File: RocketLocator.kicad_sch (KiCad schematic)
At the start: 102 parts, among them J1 USB_C, J12 Battery / Switch, J2 Deploy Ch1 / Ch2, J3 Battery-, J4 Deploy Ch3 / Ch4, J7 U.FL-R-SMT(01), J8 Conn_ST_STDC14, Q1 2N7002KN, Q3 BSS84, U1 TPS22950YBHR, U11 PAM8904EGPR, U12 74HCS00, U13 DMP2021UFDF, U14 ISM6HG256XTR, U15 TPS22950YBHR, U16 MS5611-01BA, U17 MX25L6436F, U18 BQ25185DLHR, U2 SAM-M10Q-00B, U3 DRV5032DUDMRR, U4 CH340N, U5 STM32WL5MOCH6TR, U6 TPS22950YBHR, U7 RT9080-33GJ5, U8 TPS22950YBHR, U9 TPS22950YBHR

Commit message: Bundle project symbol and footprint libraries (#10)
* Bundle project symbol and footprint libraries

Adds the Custom symbol and footprint libraries from the personal KiCad 9.0
library folder, plus RT9080-33GJ5, STM32WL5MOCH6TR and U.FL-R-SMT_01_
symbols extracted from the schematic's embedded cache. Registers them in
project lib tables via ${KIPRJMOD} and adds a CI step that loads every
library so a broken file fails the build.

Co-Authored-By: Claude Opus 5.5 (1M context) <noreply@anthropic.com>
Claude-Session: https://claude.ai/code/session_01C1wUevCmefHv8PBPpeosyX

* Recover U7 and U17 footprints into Custom.pretty and relink

The RT9080 and Package_SO_New libraries are gone, so the footprints
were extracted from RocketLocator.kicad_pcb, un-flipped from B.Cu to
library (F.Cu) form, and added to lib/Custom.pretty. The schematic,
PCB and RT9080-33GJ5 symbol now point at Custom:.

Co-Authored-By: Claude Opus 5.5 (1M context) <noreply@anthropic.com>
Claude-Session: https://claude.ai/code/session_01C1wUevCmefHv8PBPpeosyX

---------

Co-authored-by: Claude <noreply@anthropic.com>
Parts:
- U17: footprint Package_SO_New:SOP-8_5.28x5.23mm_P1.27mm -> Custom:SOP-8_5.28x5.23mm_P1.27mm
- U7: footprint RT9080:SOT94P280X100-5N -> Custom:SOT94P280X100-5N
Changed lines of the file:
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@@
 			)
 		)
-		(property "Footprint" "RT9080:SOT94P280X100-5N"
+		(property "Footprint" "Custom:SOT94P280X100-5N"
 			(at 237.49 35.56 0)
 			(hide yes)
@@
 			)
 		)
-		(property "Footprint" "Package_SO_New:SOP-8_5.28x5.23mm_P1.27mm"
+		(property "Footprint" "Custom:SOP-8_5.28x5.23mm_P1.27mm"
 			(at 379.73 231.14 0)
 			(hide yes)

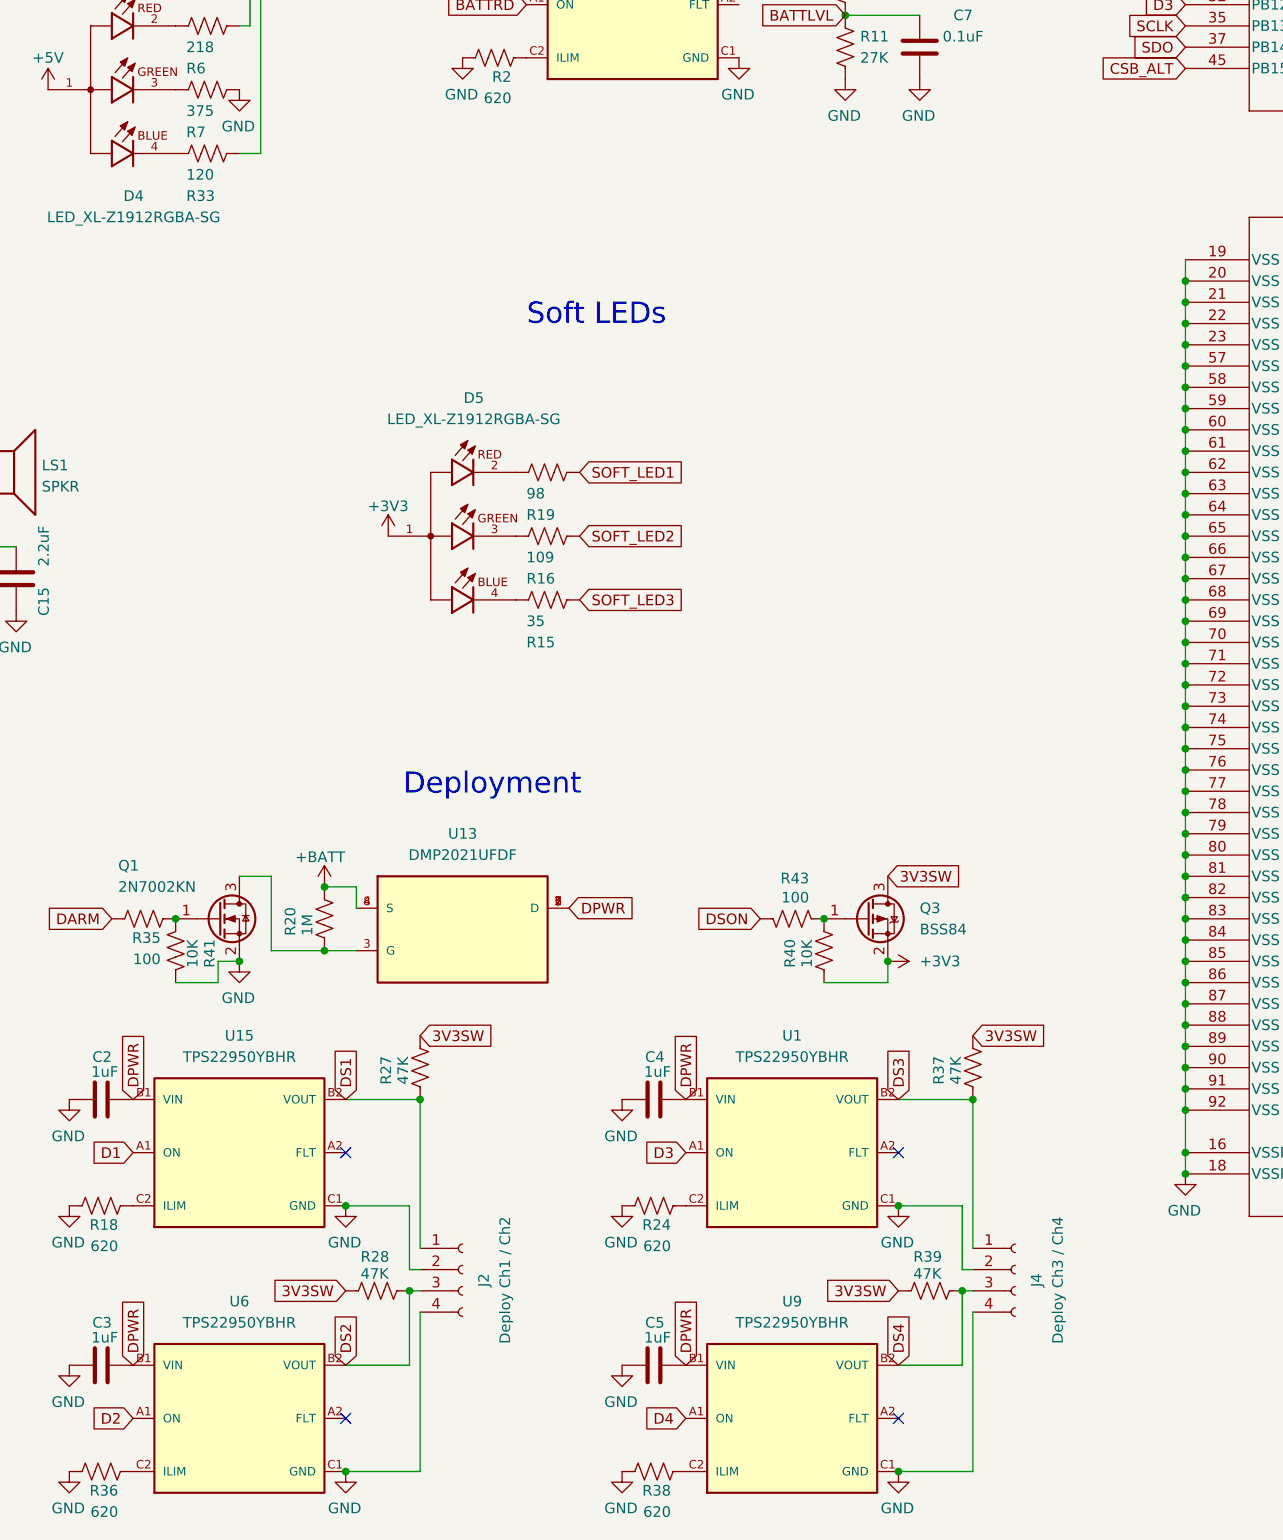
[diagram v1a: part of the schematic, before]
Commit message: Switch deploy returns low-side so continuity sense works (Topology A)
Each deploy channel's e-match return (J2/J4 pins 2 and 4) now goes through
an AO3400A low-side N-FET (Q4-Q7) instead of straight to GND. The gate is
driven from the same Dn GPIO as the TPS22950 ON pin through 100R, with a
100K pull-down. The DSn sense net and its existing 47K pull-up (R27, R28,
R37, R39) move to the FET drain, so the TPS22950 quick output discharge no
longer pins the sense node low. Each TPS22950 output (now DEPLOYn+) gets a
1K bleeder to GND (R53-R56).

The Soft LEDs block moved 25.4 mm left to make room for the new block.
The PCB still needs Update PCB from Schematic, placement and routing.

Fixes #1

Co-Authored-By: Claude Opus 5.5 (1M context) <noreply@anthropic.com>
Claude-Session: https://claude.ai/code/session_01MkgwVw8wg6ywYfkGV7BwAK
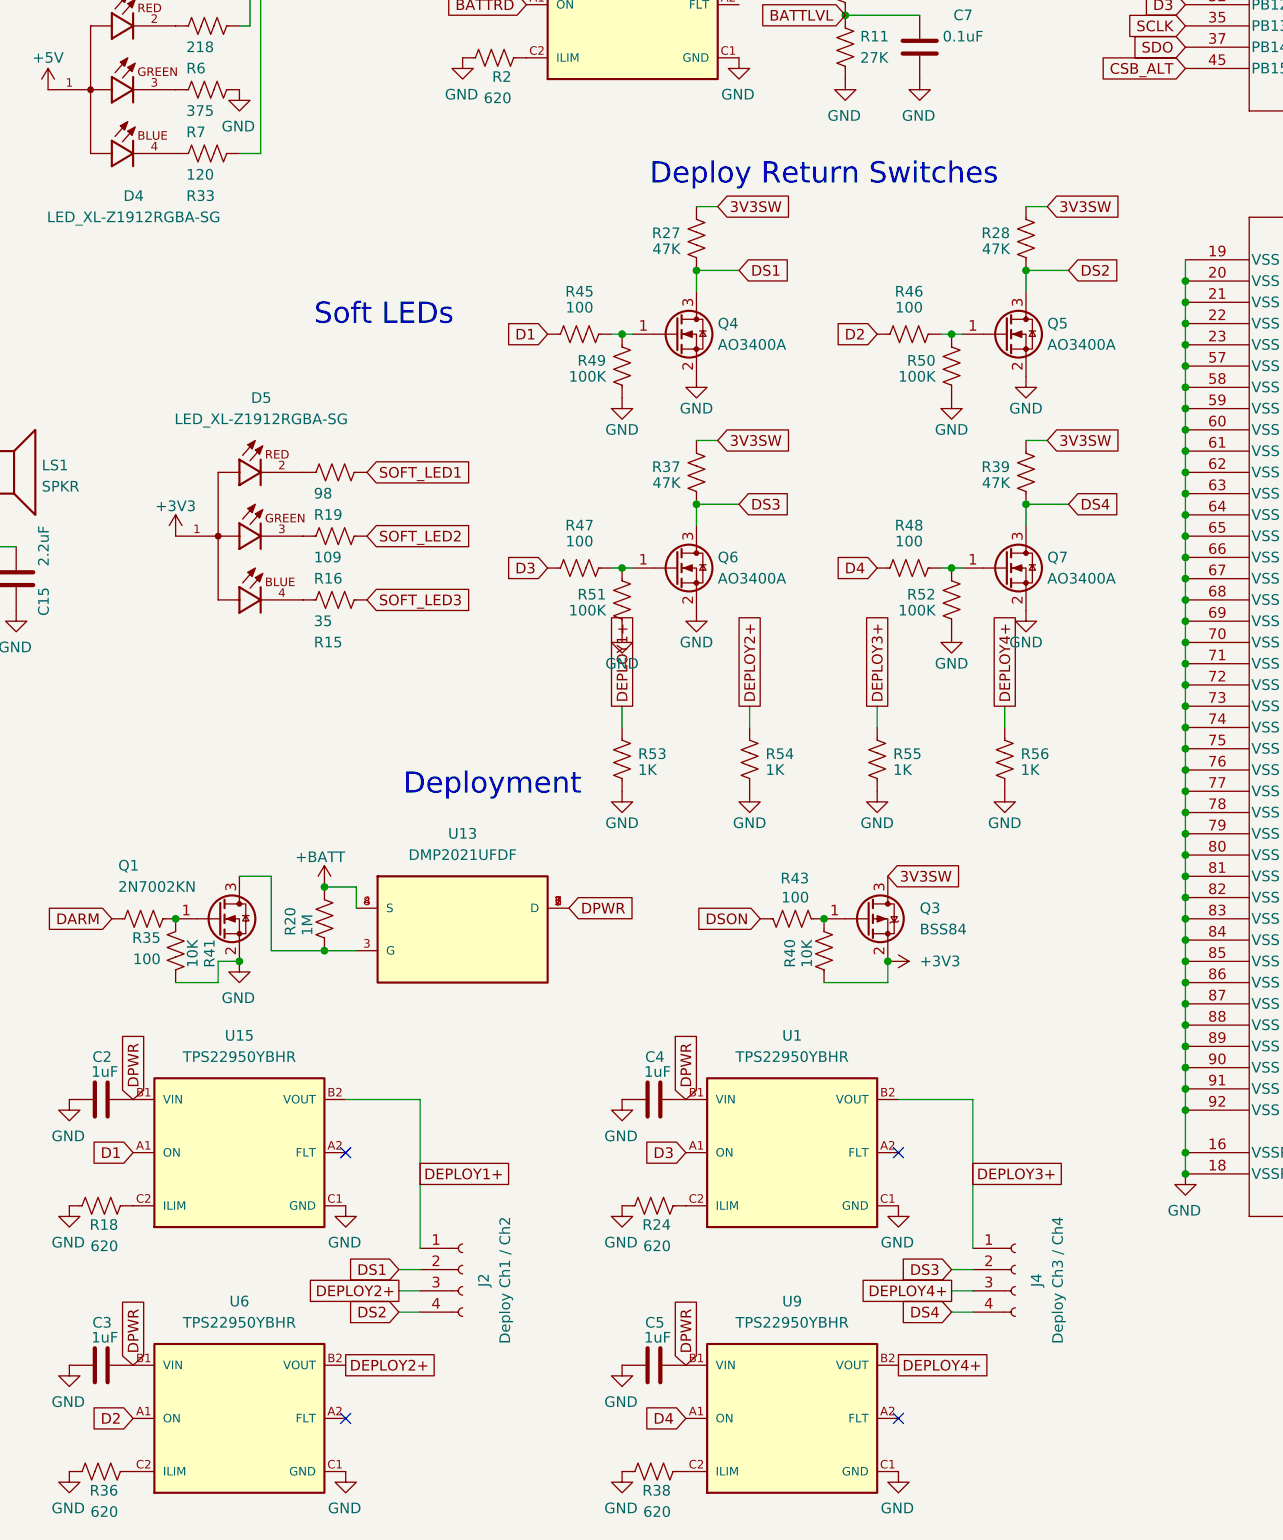
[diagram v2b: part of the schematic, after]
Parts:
- added Q4, Q5, Q6, Q7: AO3400A, Package_TO_SOT_SMD:SOT-23, symbol Transistor_FET:AO3400A
- added R45, R46, R47, R48: 100, Resistor_SMD:R_0402_1005Metric, symbol Device:R_US
- added R49, R50, R51, R52: 100K, Resistor_SMD:R_0402_1005Metric, symbol Device:R_US
- added R53, R54, R55, R56: 1K, Resistor_SMD:R_0402_1005Metric, symbol Device:R_US
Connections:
- net D1: now also R45.2
- net D2: now also R46.2
- net D3: now also R47.2
- net D4: now also R48.2
- net DS1: now also J2.2 (Pin_2), Q4.3 (D); no longer J2.1 (Pin_1), U15.B2 (VOUT)
- net DS2: now also J2.4 (Pin_4), Q5.3 (D); no longer J2.3 (Pin_3), U6.B2 (VOUT)
- net DS3: now also J4.2 (Pin_2), Q6.3 (D); no longer J4.1 (Pin_1), U1.B2 (VOUT)
- net DS4: now also J4.4 (Pin_4), Q7.3 (D); no longer J4.3 (Pin_3), U9.B2 (VOUT)
- net GND: now also Q4.2 (S), Q5.2 (S), Q6.2 (S), Q7.2 (S), R49.2, R50.2, R51.2, R52.2, R53.2, R54.2, R55.2, R56.2; no longer J2.2 (Pin_2), J2.4 (Pin_4), J4.2 (Pin_2), J4.4 (Pin_4)
- new net: Q5.1 (G), R46.1, R50.1
- new net: Q4.1 (G), R45.1, R49.1
- new net: Q7.1 (G), R48.1, R52.1
- new net: Q6.1 (G), R47.1, R51.1
- new net DEPLOY1+: J2.1 (Pin_1), R53.1, U15.B2 (VOUT)
- new net DEPLOY2+: J2.3 (Pin_3), R54.1, U6.B2 (VOUT)
- new net DEPLOY3+: J4.1 (Pin_1), R55.1, U1.B2 (VOUT)
- new net DEPLOY4+: J4.3 (Pin_3), R56.1, U9.B2 (VOUT)
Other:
- note added: "Deploy Return Switches"
- moved on the sheet: D5, R15, R16, R19, R27, R28, R37, R39

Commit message: Use PMXB43UNE (DFN1010D-3) for the deploy return switches
Q4-Q7 change from AO3400A (SOT-23) to Nexperia PMXB43UNE: 20 V, 3.2 A,
68 mOhm max at Vgs 2.5 V, 1.1 x 1.0 mm, so two fit beside J4 on the
bottom side. Adds lib/Custom.pretty/Nexperia_DFN1010D-3_SOT1215 built
from the datasheet's reflow footprint (Fig. 20): 0.35 x 0.4 mm lands,
0.25 x 0.3 mm paste, 0.45 x 0.5 mm resist; the centre drain bar has no
land. Symbol is the stock Transistor_FET:Q_NMOS_GSD (1=G, 2=S, 3=D).

Also turns the bleeder DEPLOYn+ labels horizontal so they no longer
overlap the GND symbols above them.

Co-Authored-By: Claude Opus 5.5 (1M context) <noreply@anthropic.com>
Claude-Session: https://claude.ai/code/session_01MkgwVw8wg6ywYfkGV7BwAK
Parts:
- Q4, Q5, Q6, Q7: value AO3400A -> PMXB43UNE; footprint Package_TO_SOT_SMD:SOT-23 -> Custom:Nexperia_DFN1010D-3_SOT1215; symbol Transistor_FET:AO3400A -> Transistor_FET:Q_NMOS_GSD
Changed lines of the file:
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@@
 	)
 	(symbol
-		(lib_id "Transistor_FET:AO3400A")
+		(lib_id "Transistor_FET:Q_NMOS_GSD")
 		(at 232.41 139.7 0)
 		(unit 1)
@@
 			)
 		)
-		(property "Value" "AO3400A"
+		(property "Value" "PMXB43UNE"
 			(at 237.49 140.97 0)
 			(show_name no)
@@
 			)
 		)
-		(property "Footprint" "Package_TO_SOT_SMD:SOT-23"
+		(property "Footprint" "Custom:Nexperia_DFN1010D-3_SOT1215"
 			(at 237.49 141.605 0)
 			(hide yes)
@@
 			)
 		)
-		(property "Datasheet" "http://www.aosmd.com/pdfs/datasheet/AO3400A.pdf"
+		(property "Datasheet" "https://assets.nexperia.com/documents/data-sheet/PMXB43UNE.pdf"
 			(at 237.49 143.51 0)
 			(hide yes)
@@
 			)
 		)
-		(property "Description" "30V Vds, 5.7A Id, N-Channel MOSFET, SOT-23"
+		(property "Description" "20V Vds, 3.2A Id, 68 mOhm max at Vgs 2.5V, N-channel MOSFET, DFN1010D-3 (LCSC C547273)"
 			(at 232.41 139.7 0)
 			(hide yes)
@@
 	)
 	(symbol
-		(lib_id "Transistor_FET:AO3400A")
+		(lib_id "Transistor_FET:Q_NMOS_GSD")
 		(at 271.78 139.7 0)
 		(unit 1)
@@
 			)
 		)
-		(property "Value" "AO3400A"
+		(property "Value" "PMXB43UNE"
 			(at 276.86 140.97 0)
 			(show_name no)
@@
 			)
 		)
-		(property "Footprint" "Package_TO_SOT_SMD:SOT-23"
+		(property "Footprint" "Custom:Nexperia_DFN1010D-3_SOT1215"
 			(at 276.86 141.605 0)
 			(hide yes)
@@
 			)
 		)
-		(property "Datasheet" "http://www.aosmd.com/pdfs/datasheet/AO3400A.pdf"
+		(property "Datasheet" "https://assets.nexperia.com/documents/data-sheet/PMXB43UNE.pdf"
 			(at 276.86 143.51 0)
 			(hide yes)
@@
 			)
 		)
-		(property "Description" "30V Vds, 5.7A Id, N-Channel MOSFET, SOT-23"
+		(property "Description" "20V Vds, 3.2A Id, 68 mOhm max at Vgs 2.5V, N-channel MOSFET, DFN1010D-3 (LCSC C547273)"
 			(at 271.78 139.7 0)
 			(hide yes)
@@
 	)
 	(symbol
-		(lib_id "Transistor_FET:AO3400A")
+		(lib_id "Transistor_FET:Q_NMOS_GSD")
 		(at 232.41 167.64 0)
 		(unit 1)
@@
 			)
 		)
-		(property "Value" "AO3400A"
+		(property "Value" "PMXB43UNE"
 			(at 237.49 168.91 0)
 			(show_name no)
@@
 			)
 		)
-		(property "Footprint" "Package_TO_SOT_SMD:SOT-23"
+		(property "Footprint" "Custom:Nexperia_DFN1010D-3_SOT1215"
 			(at 237.49 169.545 0)
 			(hide yes)
@@
 			)
 		)
-		(property "Datasheet" "http://www.aosmd.com/pdfs/datasheet/AO3400A.pdf"
+		(property "Datasheet" "https://assets.nexperia.com/documents/data-sheet/PMXB43UNE.pdf"
 			(at 237.49 171.45 0)
 			(hide yes)
@@
 			)
 		)
-		(property "Description" "30V Vds, 5.7A Id, N-Channel MOSFET, SOT-23"
+		(property "Description" "20V Vds, 3.2A Id, 68 mOhm max at Vgs 2.5V, N-channel MOSFET, DFN1010D-3 (LCSC C547273)"
 			(at 232.41 167.64 0)
 			(hide yes)
@@
 	)
 	(symbol
-		(lib_id "Transistor_FET:AO3400A")
+		(lib_id "Transistor_FET:Q_NMOS_GSD")
 		(at 271.78 167.64 0)
 		(unit 1)
@@
 			)
 		)
-		(property "Value" "AO3400A"
+		(property "Value" "PMXB43UNE"
 			(at 276.86 168.91 0)
 			(show_name no)
@@
 			)
 		)
-		(property "Footprint" "Package_TO_SOT_SMD:SOT-23"
+		(property "Footprint" "Custom:Nexperia_DFN1010D-3_SOT1215"
 			(at 276.86 169.545 0)
 			(hide yes)
@@
 			)
 		)
-		(property "Datasheet" "http://www.aosmd.com/pdfs/datasheet/AO3400A.pdf"
+		(property "Datasheet" "https://assets.nexperia.com/documents/data-sheet/PMXB43UNE.pdf"
 			(at 276.86 171.45 0)
 			(hide yes)
@@
 			)
 		)
-		(property "Description" "30V Vds, 5.7A Id, N-Channel MOSFET, SOT-23"
+		(property "Description" "20V Vds, 3.2A Id, 68 mOhm max at Vgs 2.5V, N-channel MOSFET, DFN1010D-3 (LCSC C547273)"
 			(at 271.78 167.64 0)
 			(hide yes)
@@
 	(global_label "DEPLOY1+"
 		(shape passive)
-		(at 226.06 184.15 90)
+		(at 226.06 184.15 0)
 		(fields_autoplaced yes)
 		(effects
@@
 	(global_label "DEPLOY2+"
 		(shape passive)
-		(at 241.3 184.15 90)
+		(at 241.3 184.15 0)
 		(fields_autoplaced yes)
 		(effects
@@
 	(global_label "DEPLOY3+"
 		(shape passive)
-		(at 256.54 184.15 90)
+		(at 256.54 184.15 0)
 		(fields_autoplaced yes)
 		(effects
@@
 	(global_label "DEPLOY4+"
 		(shape passive)
-		(at 271.78 184.15 90)
+		(at 271.78 184.15 0)
 		(fields_autoplaced yes)
 		(effects

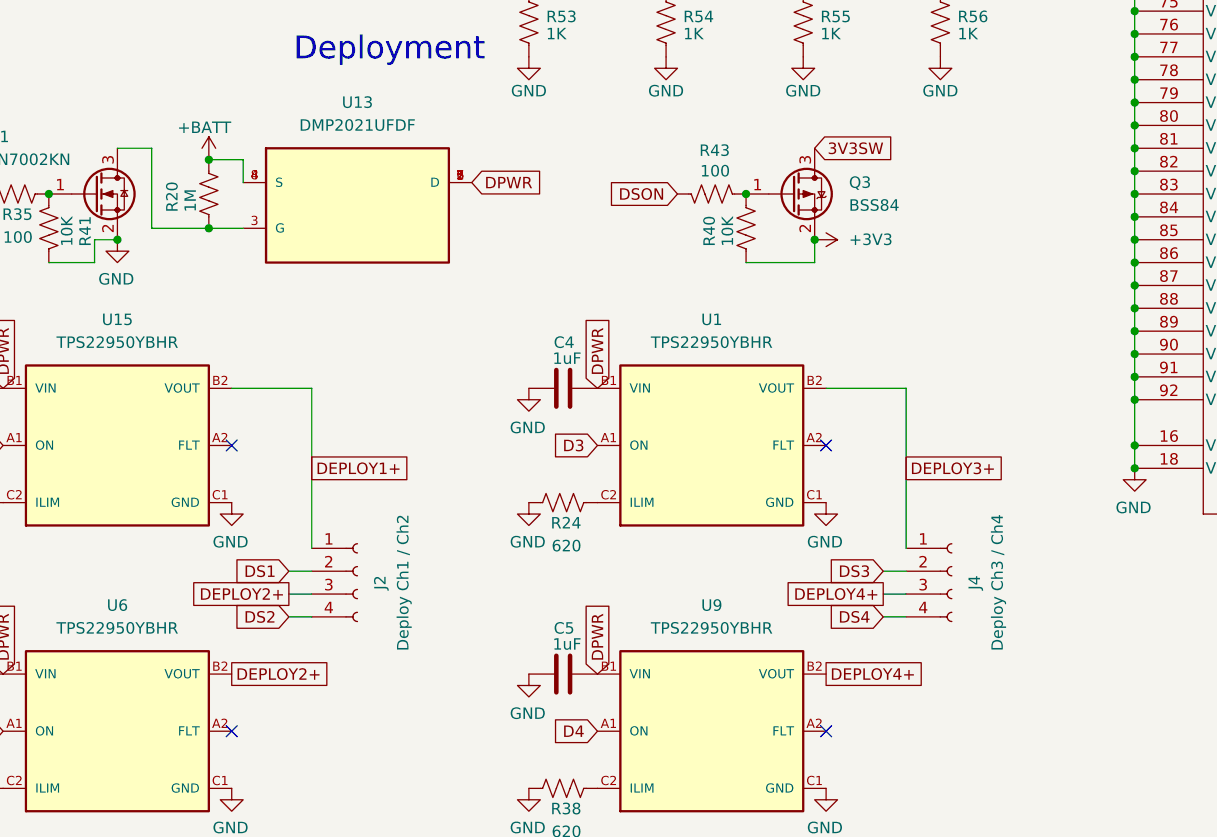
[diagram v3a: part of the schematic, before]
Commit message: Swap J2/J4 deploy pinout, lower arm-gate pull-up, fix DRC errors
Schematic:
- J2 ch2 and J4 ch3/ch4 pin order changed: J2 pin 3 = DS2,
  pin 4 = DEPLOY2+; J4 pin 1 = DS3, pin 2 = DEPLOY3+, pin 3 = DS4,
  pin 4 = DEPLOY4+.
- R20 (U13 arm FET gate pull-up) 1M -> 100K.

PCB:
- Rerouted the deploy connectors for the new pinout.
- Connected Q5 pad 2 GND, which sat on an isolated B.Cu pour island
  (DRC "missing connection" on the GND zone).
- Updated U5 from the fixed LGA-92 library footprint (malformed
  courtyard errors).

DRC now reports no errors and no unconnected items. The remaining
ERC errors predate this change.

Co-Authored-By: Claude Opus 5.5 (1M context) <noreply@anthropic.com>
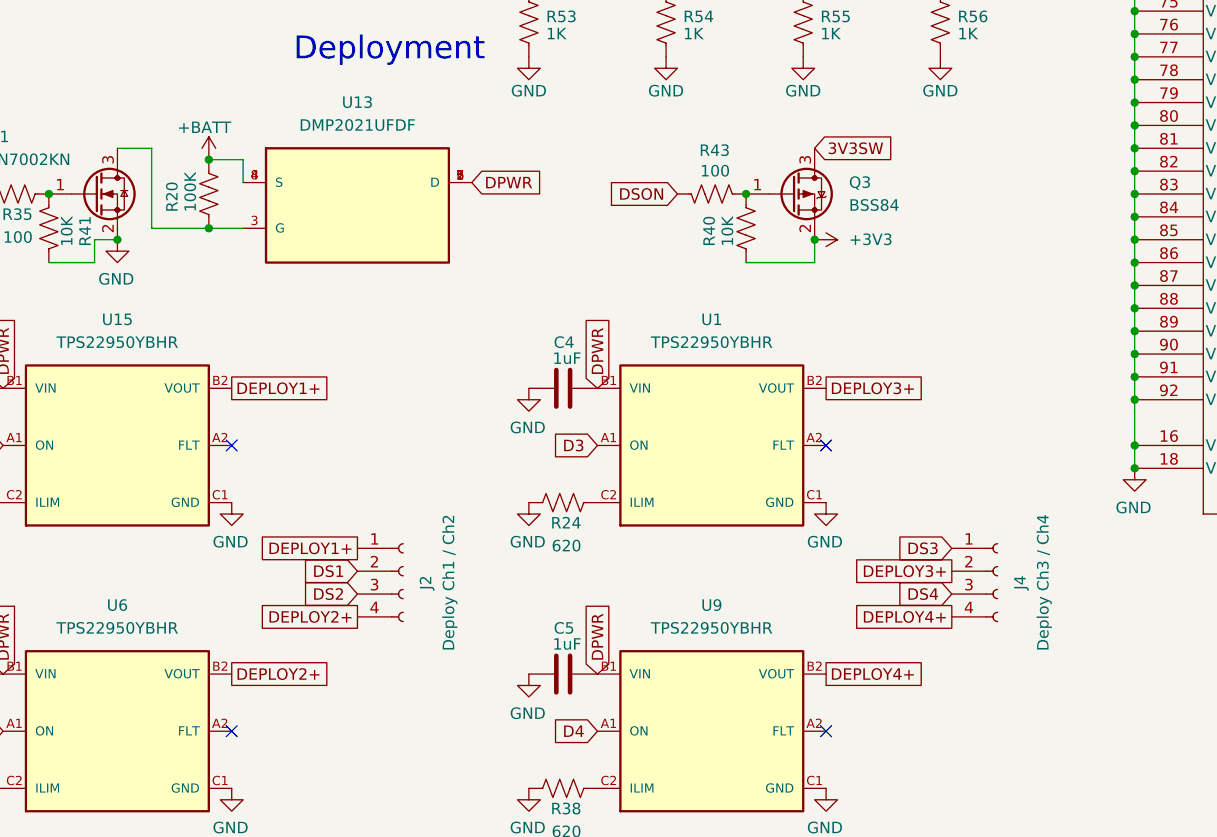
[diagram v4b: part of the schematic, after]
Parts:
- R20: value 1M -> 100K
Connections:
- net DEPLOY2+: now also J2.4 (Pin_4); no longer J2.3 (Pin_3)
- net DEPLOY3+: now also J4.2 (Pin_2); no longer J4.1 (Pin_1)
- net DEPLOY4+: now also J4.4 (Pin_4); no longer J4.3 (Pin_3)
- net DS2: now also J2.3 (Pin_3); no longer J2.4 (Pin_4)
- net DS3: now also J4.1 (Pin_1); no longer J4.2 (Pin_2)
- net DS4: now also J4.3 (Pin_3); no longer J4.4 (Pin_4)
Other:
- moved on the sheet: J2, J4
